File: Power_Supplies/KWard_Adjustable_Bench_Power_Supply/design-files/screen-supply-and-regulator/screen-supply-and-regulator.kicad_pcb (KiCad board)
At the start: 2 copper layers, 156.2 x 102.9 mm, 42 parts, among them J1 120VAC, J2 Tube Pass Array, J3 Meters, J4 To Panel Jacks, Q1 STP16N50M2, SW1 I-meter bypass, SW2 DUT discharge, U1 LM317

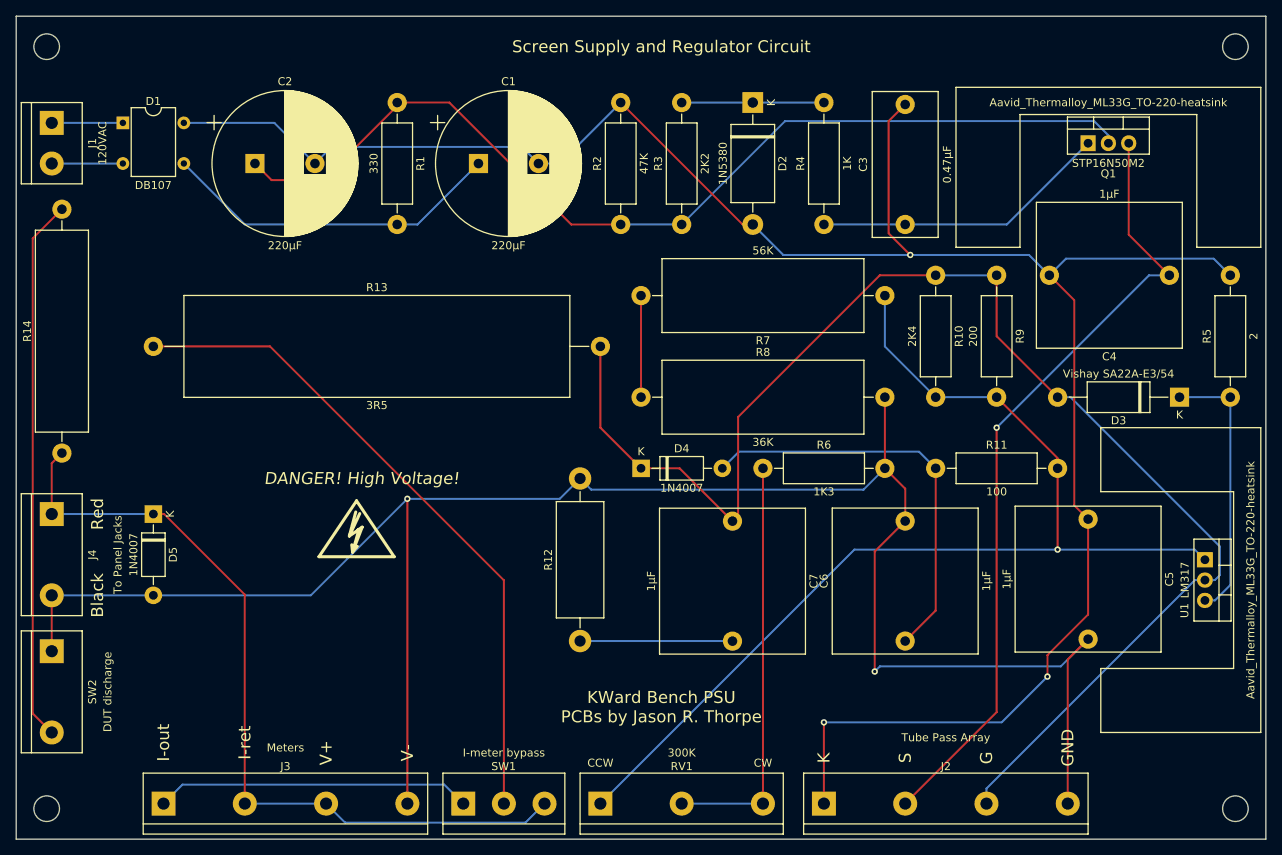
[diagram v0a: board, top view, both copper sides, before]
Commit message: Minor tweaks to the silk screen on the regulator board.
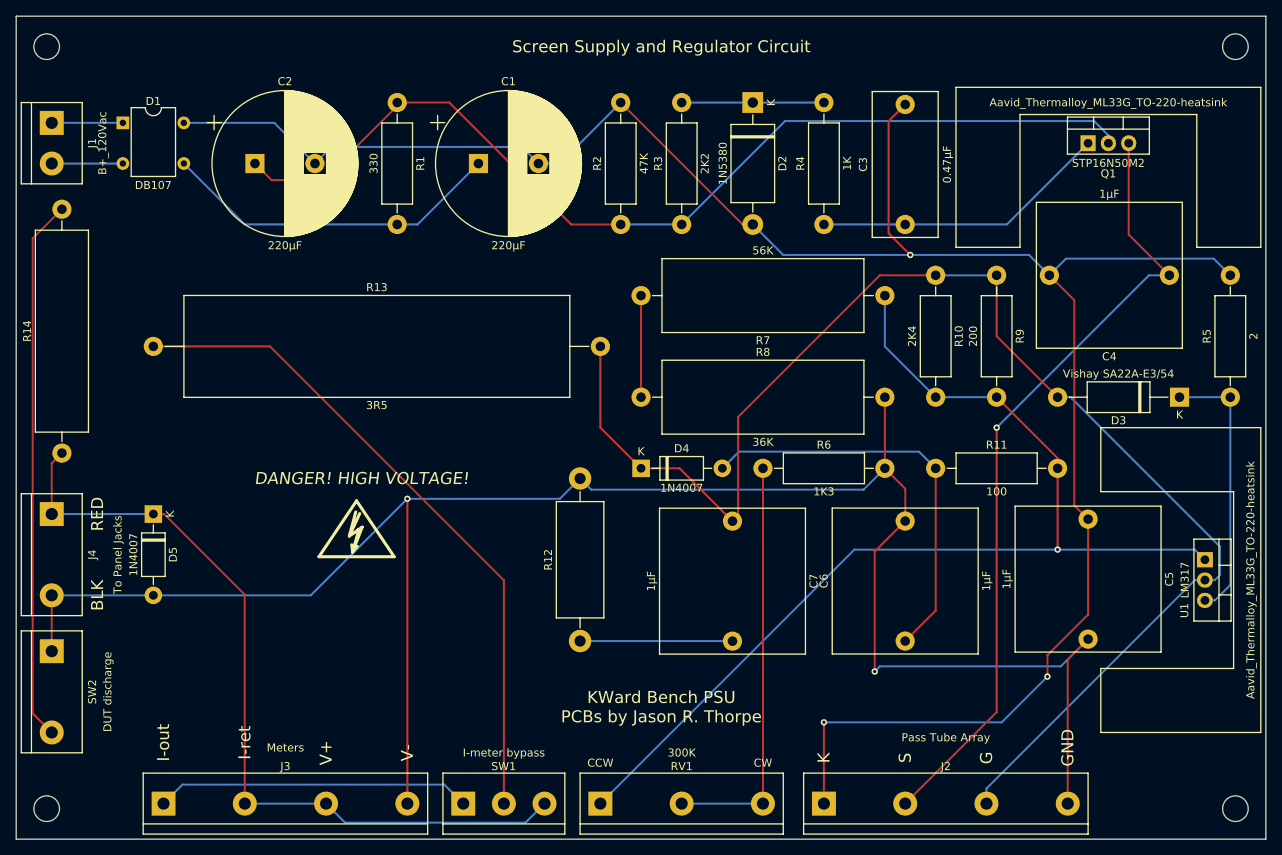
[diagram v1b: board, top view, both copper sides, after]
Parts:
- J1: value 120VAC -> B+_120Vac
- J2: value Tube Pass Array -> Pass Tube Array
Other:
- board text added: "BLK"
- board text added: "DANGER! HIGH VOLTAGE!"
- board text added: "RED"
- board text removed: "Black"
- board text removed: "DANGER! High Voltage!"
- board text removed: "Red"

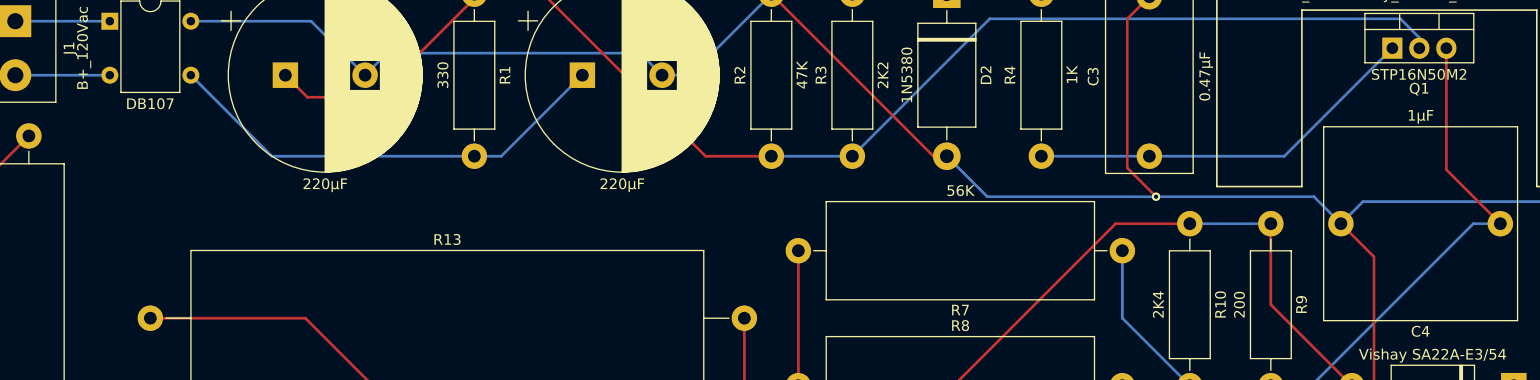
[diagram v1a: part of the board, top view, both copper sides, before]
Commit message: Part # tweaks (to reflect currently-available components).
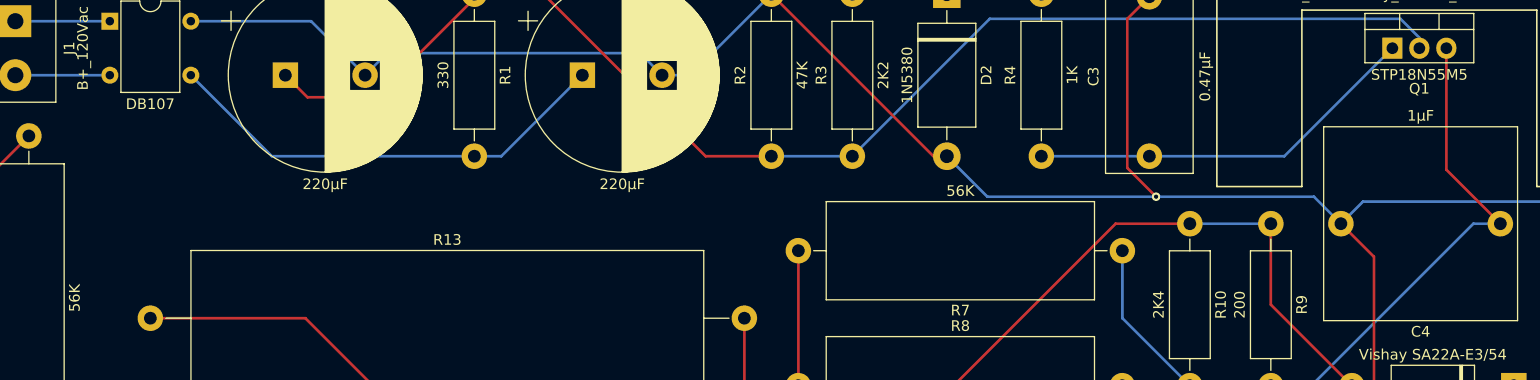
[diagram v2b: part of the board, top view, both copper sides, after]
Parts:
- Q1: value STP16N50M2 -> STP18N55M5
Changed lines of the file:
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@@
       (effects (font (size 1 1) (thickness 0.15)))
     )
-    (fp_text value STP16N50M2 (at 2.54 2.5) (layer F.SilkS)
+    (fp_text value STP18N55M5 (at 2.54 2.5) (layer F.SilkS)
       (effects (font (size 1 1) (thickness 0.15)))
     )
@@
       (effects (font (size 1 1) (thickness 0.15)))
     )
-    (fp_text value 56K (at 15.24 4.32 90) (layer F.Fab)
-      (effects (font (size 1 1) (thickness 0.15)))
-    )
+    (fp_text value 56K (at 15.24 4.32 90) (layer F.SilkS)
+      (effects (font (size 1 1) (thickness 0.15)))
+    )
